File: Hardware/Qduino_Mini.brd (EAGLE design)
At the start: 20.3 x 38.1 mm, 41 parts, among them J1 LiPo, Q1 PFET, U1 ATMEGA32U41:1-LESS_PASTE, U2 MCP73831, U3 MAX17048, U4 AP2112K-3.3TRG-1, U5 MIGHTYQ-L-SILK, Y1 8MHZ

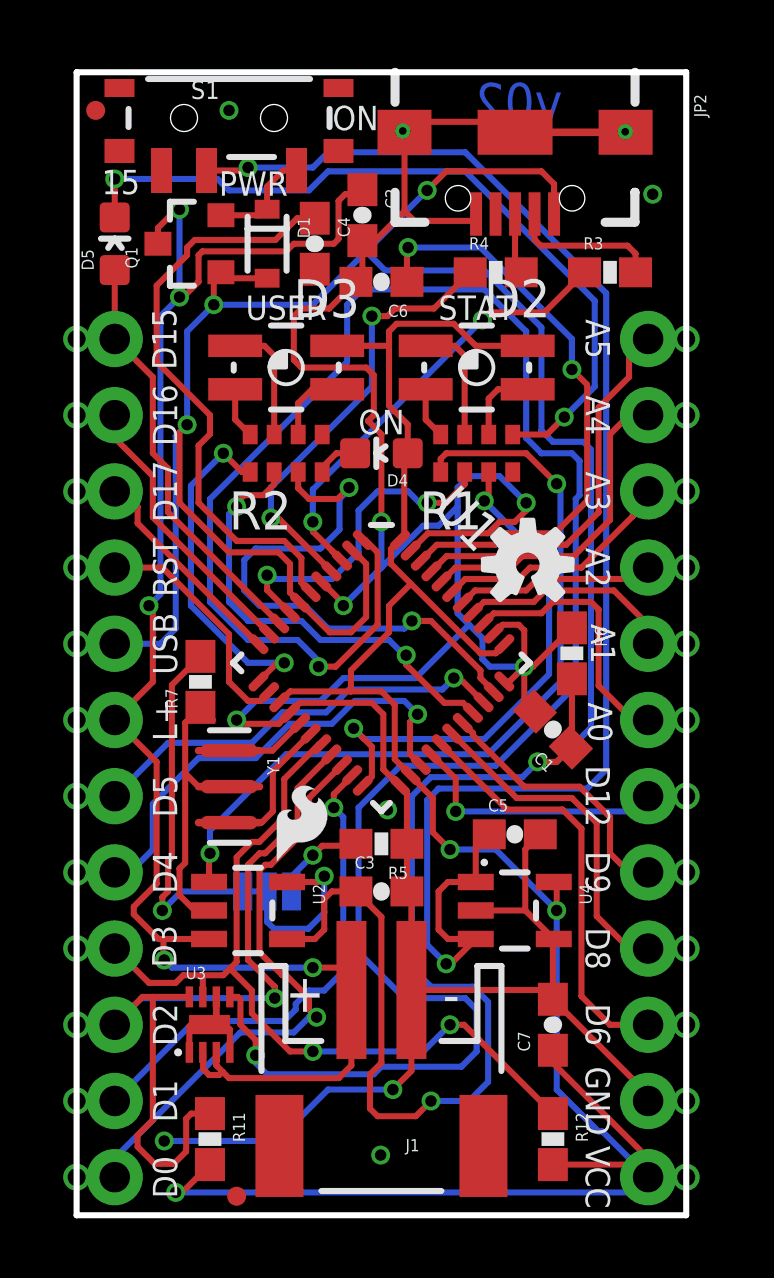
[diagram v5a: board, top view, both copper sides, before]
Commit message: moved some traces around to make them shorter
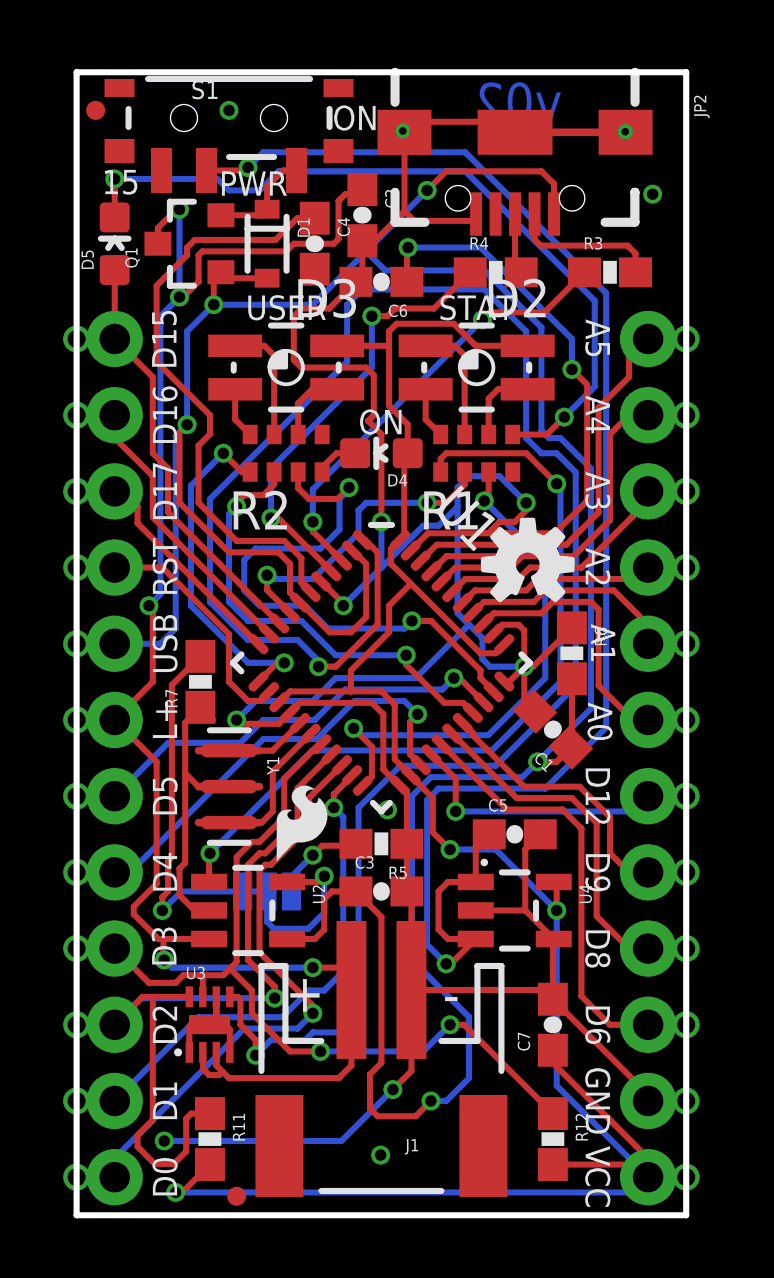
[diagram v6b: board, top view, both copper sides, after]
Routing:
- net !ALRT: track 72.4 -> 63.8 mm
- net VBUS: track 106.2 -> 103.7 mm
- net D4: track 16.8 -> 15.9 mm
- net VINPUT: track 50.6 -> 49.8 mm
- net TXLED: track 11.1 -> 10.4 mm

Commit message: Removed 4th for-the-user LED, D5 & its current limit resistor
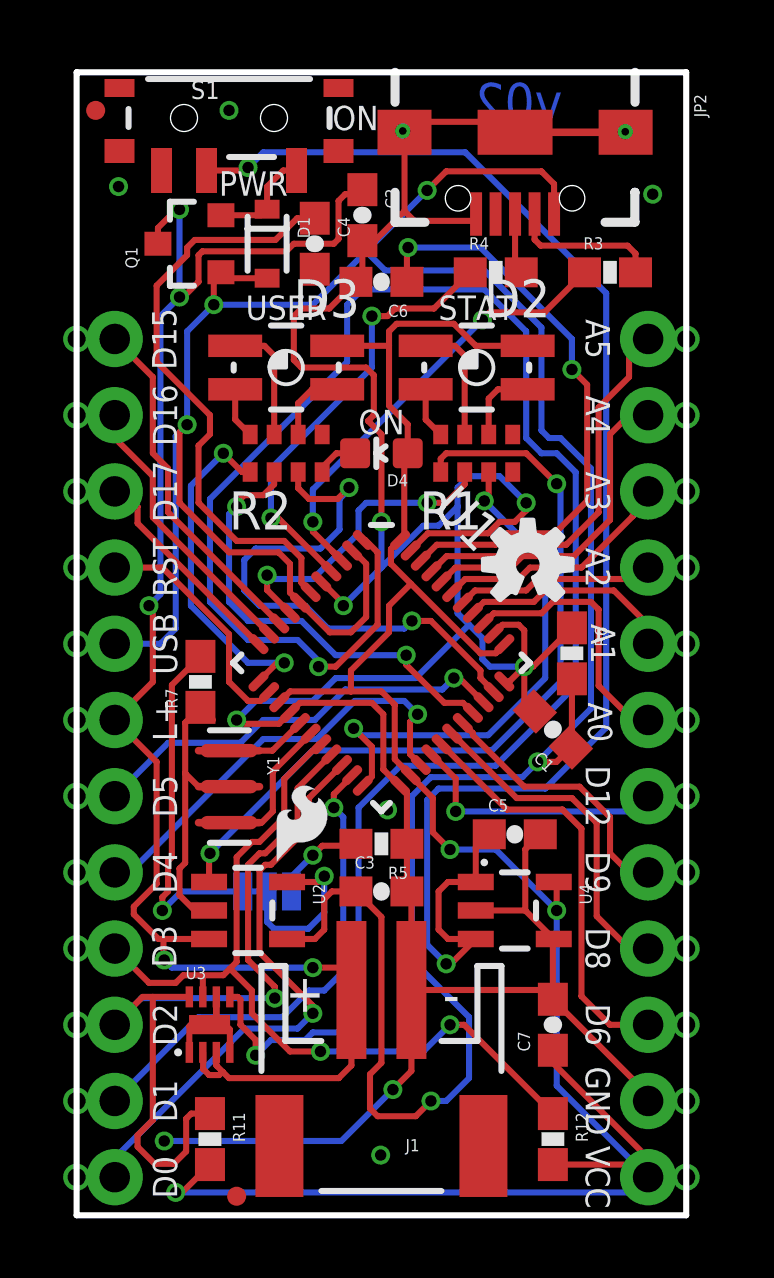
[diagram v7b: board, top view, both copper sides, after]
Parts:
- removed D5: Yellow, SparkFun-LED:LED-0603
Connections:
- removed net N$5: D5.C, R1.5
- net GND: no longer R1.4
- net SCK: no longer D5.A
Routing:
- net N$5: track 25.7 -> 0.00 mm, vias 2 -> 0
- net SCK: track 15.3 -> 13.0 mm
- net GND: vias 12 -> 13
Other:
- board text removed: "15"
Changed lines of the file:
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@@
 <?xml version="1.0" encoding="utf-8"?>
 <!DOCTYPE eagle SYSTEM "eagle.dtd">
-<eagle version="7.1.0">
+<eagle version="7.2.0">
 <drawing>
 <settings>
@@
 <text x="6.985" y="29.845" size="0.8128" layer="21" font="vector" ratio="15" align="bottom-center">USER</text>
 <text x="13.335" y="29.845" size="0.8128" layer="21" font="vector" ratio="15" align="bottom-center">STAT</text>
-<text x="1.4732" y="34.036" size="0.8128" layer="21" font="vector" ratio="15" align="bottom-center">15</text>
 <text x="10.1854" y="2.8448" size="1.016" layer="22" ratio="15" rot="MR0" align="center">Qduino Mini</text>
 <text x="6.35" y="12.0396" size="0.8128" layer="22" font="vector" ratio="16" rot="SMR0" align="bottom-center">SJ1</text>
@@
 <attribute name="PROD_ID" value="DIO-00821" x="10.16" y="25.4" size="1.778" layer="27" rot="R90" display="off"/>
 </element>
-<element name="D5" library="SparkFun-LED" package="LED-0603" value="Yellow" x="1.27" y="32.385">
-<attribute name="PROD_ID" value="DIO-09003" x="1.27" y="32.385" size="1.778" layer="27" display="off"/>
-</element>
 <element name="U2" library="SparkFun" package="SOT23-5" value="MCP73831" x="5.715" y="10.16" rot="R270">
 <attribute name="PROD_ID" value="IC-09995" x="5.715" y="10.16" size="1.778" layer="27" rot="R270" display="off"/>
@@
 <wire x1="14.615" y1="36.1" x2="18.3" y2="36.1" width="0.254" layer="1"/>
 <contactref element="JP3" pad="2"/>
-<contactref element="R1" pad="4"/>
 <via x="20.32" y="3.81" extent="1-16" drill="0.6"/>
 <wire x1="10.93" y1="36.1" x2="11.081" y2="36.1" width="0.2032" layer="1"/>
@@
 <via x="19.2024" y="34.036" extent="1-16" drill="0.381"/>
 <via x="10.3632" y="13.5128" extent="1-16" drill="0.381"/>
+<via x="1.397" y="34.29" extent="1-16" drill="0.381"/>
 </signal>
 <signal name="!RST">
@@
 <signal name="SCK">
 <contactref element="U1" pad="9"/>
-<contactref element="D5" pad="A"/>
 <contactref element="JP4" pad="12"/>
 <via x="0" y="29.21" extent="1-16" drill="0.6"/>
 <wire x1="0" y1="29.21" x2="1.27" y2="29.21" width="0.2032" layer="1"/>
-<wire x1="1.27" y1="31.508" x2="1.27" y2="29.21" width="0.2032" layer="1"/>
 <wire x1="3.048" y1="23.435559375" x2="6.75501875" y2="19.728540625" width="0.2032" layer="1"/>
 <wire x1="3.048" y1="23.435559375" x2="3.048" y2="24.892" width="0.2032" layer="1"/>
@@
 <wire x1="5.285" y1="28.9825" x2="6.26" y2="28.9825" width="0.2032" layer="1"/>
 </signal>
-<signal name="N$5">
-<contactref element="D5" pad="C"/>
-<contactref element="R1" pad="5"/>
-<via x="1.27" y="34.544" extent="1-16" drill="0.381"/>
-<wire x1="1.27" y1="34.544" x2="1.27" y2="33.262" width="0.2032" layer="1"/>
-<wire x1="14.535" y1="26.025" x2="15.6745" y2="26.025" width="0.2032" layer="1"/>
-<wire x1="15.6745" y1="26.025" x2="16.256" y2="26.6065" width="0.2032" layer="1"/>
-<via x="16.256" y="26.6065" extent="1-16" drill="0.381"/>
-<wire x1="6.096" y1="34.163" x2="6.731" y2="34.798" width="0.2032" layer="16"/>
-<wire x1="1.27" y1="34.544" x2="4.699" y2="34.544" width="0.2032" layer="16"/>
-<wire x1="4.699" y1="34.544" x2="5.08" y2="34.163" width="0.2032" layer="16"/>
-<wire x1="5.08" y1="34.163" x2="6.096" y2="34.163" width="0.2032" layer="16"/>
-<wire x1="6.731" y1="34.798" x2="12.954" y2="34.798" width="0.2032" layer="16"/>
-<wire x1="12.954" y1="34.798" x2="17.272" y2="30.48" width="0.2032" layer="16"/>
-<wire x1="17.272" y1="30.48" x2="17.272" y2="27.6225" width="0.2032" layer="16"/>
-<wire x1="17.272" y1="27.6225" x2="16.256" y2="26.6065" width="0.2032" layer="16"/>
-</signal>
 <signal name="N$4">
